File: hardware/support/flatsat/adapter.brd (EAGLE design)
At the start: 26 x 19 mm, 2 parts, among them X1 FH12-40S-0.5SH

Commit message: merged master updates
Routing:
- net RTN_+3V3: track 6.58 -> 7.84 mm
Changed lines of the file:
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@@
 </signal>
 <signal name="RTN_+3V3">
+<contactref element="U$1" pad="P$53"/>
+<contactref element="U$1" pad="P$54"/>
+<contactref element="U$1" pad="P$55"/>
 <contactref element="U$1" pad="P$56"/>
-<contactref element="U$1" pad="P$55"/>
-<contactref element="U$1" pad="P$54"/>
-<contactref element="U$1" pad="P$53"/>
 <contactref element="X1" pad="14"/>
 <wire x1="16.25" y1="11.6" x2="16.25" y2="9.35" width="0.3" layer="1"/>
 <wire x1="16.25" y1="9.35" x2="17.4" y2="8.2" width="0.3" layer="1"/>
 <wire x1="17.4" y1="8.2" x2="17.4" y2="7.95" width="0.3" layer="1"/>
-<wire x1="17.4" y1="7.95" x2="17.4" y2="7.3" width="0.3" layer="1"/>
+<wire x1="17.4" y1="7.95" x2="19.2" y2="7.3" width="0.3" layer="1"/>
 <wire x1="17.4" y1="7.95" x2="19.2" y2="7.95" width="0.35" layer="1"/>
 <wire x1="18.6" y1="7.3" x2="19.2" y2="7.3" width="0" layer="19" extent="1-1"/>
-<wire x1="18" y1="7.3" x2="18.6" y2="7.3" width="0" layer="19" extent="1-1"/>
-<wire x1="17.4" y1="7.3" x2="18" y2="7.3" width="0" layer="19" extent="1-1"/>
+<wire x1="18.6" y1="7.3" x2="18.6" y2="7.3" width="0" layer="19" extent="1-1"/>
+<wire x1="19.2" y1="7.3" x2="18.6" y2="7.3" width="0" layer="19" extent="1-1"/>
 </signal>
 <signal name="RTN_BATV">
+<contactref element="U$1" pad="P$45"/>
+<contactref element="U$1" pad="P$46"/>
+<contactref element="U$1" pad="P$47"/>
 <contactref element="U$1" pad="P$48"/>
-<contactref element="U$1" pad="P$47"/>
-<contactref element="U$1" pad="P$46"/>
-<contactref element="U$1" pad="P$45"/>
 <contactref element="X1" pad="16"/>
 <wire x1="15.25" y1="11.6" x2="15.25" y2="9.05" width="0.3" layer="1"/>
@@
 <wire x1="14.4" y1="7.95" x2="14.4" y2="7.3" width="0.3" layer="1"/>
 <wire x1="14.4" y1="7.95" x2="12.6" y2="7.95" width="0.35" layer="1"/>
-<wire x1="13.2" y1="7.3" x2="13.8" y2="7.3" width="0" layer="19" extent="1-1"/>
+<wire x1="13.8" y1="7.3" x2="13.8" y2="7.3" width="0" layer="19" extent="1-1"/>
 <wire x1="14.4" y1="7.3" x2="13.8" y2="7.3" width="0" layer="19" extent="1-1"/>
-<wire x1="12.6" y1="7.3" x2="13.2" y2="7.3" width="0" layer="19" extent="1-1"/>
+<wire x1="14.4" y1="7.3" x2="13.8" y2="7.3" width="0" layer="19" extent="1-1"/>
 </signal>
 <signal name="GPIO10">
@@
 </signal>
 <signal name="BATV_BUS">
+<contactref element="U$1" pad="P$52"/>
+<contactref element="U$1" pad="P$51"/>
+<contactref element="U$1" pad="P$50"/>
 <contactref element="U$1" pad="P$49"/>
-<contactref element="U$1" pad="P$50"/>
-<contactref element="U$1" pad="P$51"/>
-<contactref element="U$1" pad="P$52"/>
 <contactref element="X1" pad="15"/>
 <wire x1="15.75" y1="11.6" x2="15.75" y2="8.35" width="0.3" layer="1"/>
 <wire x1="15.75" y1="8.35" x2="15.6" y2="8.2" width="0.3" layer="1"/>
 <wire x1="15.6" y1="8.2" x2="15.6" y2="7.3" width="0.3" layer="1"/>
-<wire x1="16.8" y1="7.3" x2="16.2" y2="7.3" width="0" layer="19" extent="1-1"/>
-<wire x1="15.6" y1="7.3" x2="16.2" y2="7.3" width="0" layer="19" extent="1-1"/>
+<wire x1="15" y1="7.3" x2="15.6" y2="7.3" width="0" layer="19" extent="1-1"/>
+<wire x1="15.6" y1="7.3" x2="15.6" y2="7.3" width="0" layer="19" extent="1-1"/>
 <wire x1="15" y1="7.3" x2="15.6" y2="7.3" width="0" layer="19" extent="1-1"/>
 </signal>
@@
 </signal>
 <signal name="+3V3_BUS">
+<contactref element="U$1" pad="P$60"/>
+<contactref element="U$1" pad="P$59"/>
+<contactref element="U$1" pad="P$58"/>
 <contactref element="U$1" pad="P$57"/>
-<contactref element="U$1" pad="P$58"/>
-<contactref element="U$1" pad="P$59"/>
-<contactref element="U$1" pad="P$60"/>
 <contactref element="X1" pad="13"/>
 <wire x1="16.75" y1="11.6" x2="16.75" y2="10.9" width="0.3" layer="1"/>
@@
 <wire x1="19.8" y1="7.95" x2="19.8" y2="7.3" width="0.3" layer="1"/>
 <wire x1="19.8" y1="7.95" x2="21.6" y2="7.95" width="0.35" layer="1"/>
-<wire x1="21" y1="7.3" x2="20.4" y2="7.3" width="0" layer="19" extent="1-1"/>
-<wire x1="21.6" y1="7.3" x2="21" y2="7.3" width="0" layer="19" extent="1-1"/>
+<wire x1="20.4" y1="7.3" x2="20.4" y2="7.3" width="0" layer="19" extent="1-1"/>
+<wire x1="19.8" y1="7.3" x2="20.4" y2="7.3" width="0" layer="19" extent="1-1"/>
 <wire x1="19.8" y1="7.3" x2="20.4" y2="7.3" width="0" layer="19" extent="1-1"/>
 </signal>

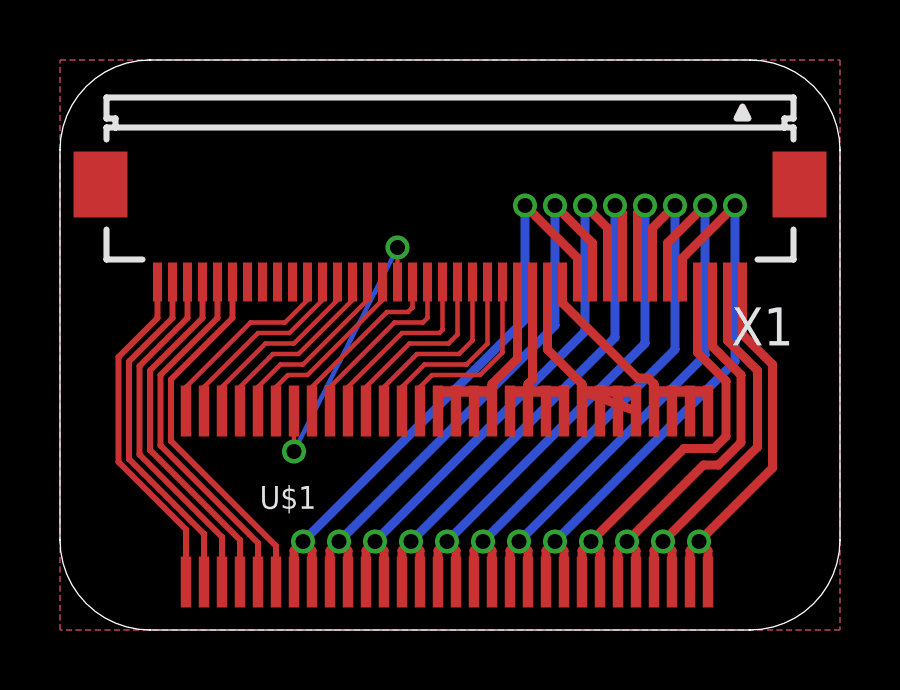
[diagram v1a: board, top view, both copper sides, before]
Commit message: added flatsat board and routed
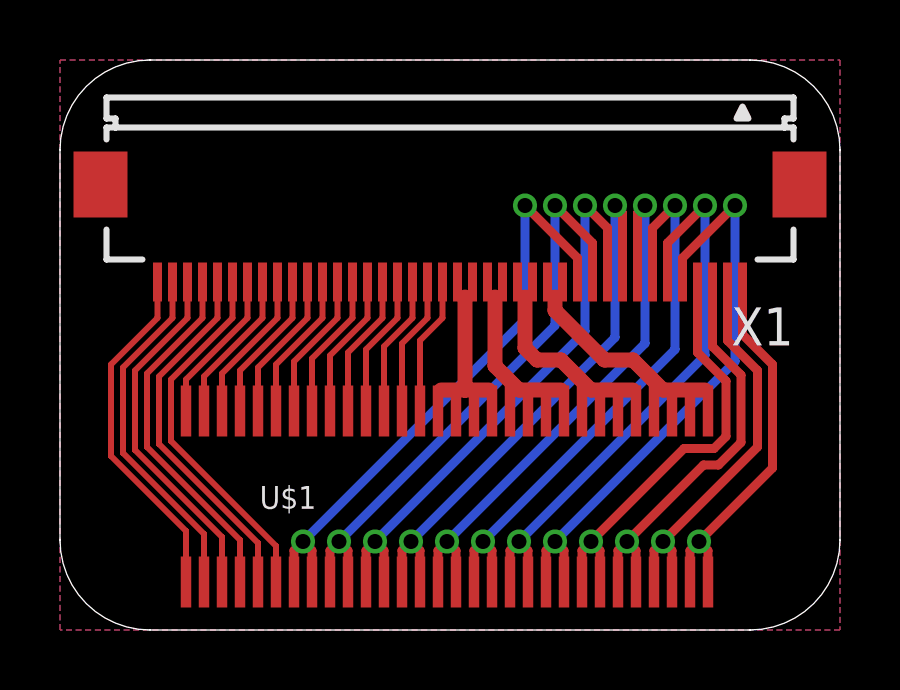
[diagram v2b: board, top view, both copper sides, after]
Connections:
- removed net +3.3V_SW1: U$1.P$2
- removed net +3V3_BUS: U$1.P$57, U$1.P$58, U$1.P$59, U$1.P$60, X1.13
- removed net BATV_BUS: U$1.P$49, U$1.P$50, U$1.P$51, U$1.P$52, X1.15
- removed net N$50: X1.31
- removed net N$51: X1.32
- removed net N$52: X1.33
- removed net N$53: X1.34
- new net +3V3: U$1.P$57, U$1.P$58, U$1.P$59, U$1.P$60, X1.13, X1.14
- new net BATV: U$1.P$49, U$1.P$50, U$1.P$51, U$1.P$52, X1.17, X1.18
- net +3V3_SW1: now also U$1.P$2
- net /SS/GPIO2: now also X1.31; no longer X1.27
- net GPIO10: now also X1.23; no longer X1.19
- net GPIO11: now also X1.22; no longer X1.18
- net GPIO12: now also X1.21; no longer X1.17
- net GPIO3: now also X1.30; no longer X1.26
- net GPIO4: now also X1.29; no longer X1.25
- net GPIO5: now also X1.28; no longer X1.24
- net GPIO6: now also X1.27; no longer X1.23
- net GPIO7: now also X1.26; no longer X1.22
- net GPIO8: now also X1.25; no longer X1.21
- net GPIO9: now also X1.24; no longer X1.20
- net MISO: now also X1.33; no longer X1.29
- net MOSI: now also X1.34; no longer X1.30
- net RTN_+3V3: now also X1.15, X1.16; no longer X1.14
- net RTN_BATV: now also X1.19, X1.20; no longer X1.16
- net SCK: now also X1.32; no longer X1.28
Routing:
- net +3V3: track 0.00 -> 8.55 mm
- net +3V3_BUS: track 7.57 -> 0.00 mm
- net BATV: track 0.00 -> 6.78 mm
- net GPIO5: track 10.1 -> 4.90 mm, vias 2 -> 0
- net BATV_BUS: track 4.36 -> 0.00 mm
- net N$32: track 1.80 -> 0.00 mm
- net GPIO12: track 6.38 -> 4.61 mm
- net GPIO10: track 6.34 -> 4.69 mm
- net GPIO11: track 6.30 -> 4.65 mm
- net GPIO9: track 6.32 -> 4.73 mm
- net GPIO8: track 6.34 -> 4.78 mm
- net MOSI: track 6.65 -> 5.15 mm
- net MISO: track 6.55 -> 5.11 mm
- net SCK: track 6.45 -> 5.07 mm
- net GPIO7: track 6.20 -> 4.82 mm
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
